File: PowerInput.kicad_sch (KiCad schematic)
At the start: 26 parts, among them J3 USB_C_Receptacle_USB2.0_16P, Q1 STL6P3LLH6, Q2 STL6P3LLH6, U4 STUSB4500QTR

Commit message: this is probably a fire hazard
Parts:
- added U5: INA180A3, Package_TO_SOT_SMD:SOT-23-5, symbol Amplifier_Current:INA180A3
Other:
- note added: "not done, pull up"
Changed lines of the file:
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@@
 	(generator_version "9.0")
 	(paper "A4")
+	(text "not done, pull up"
+		(exclude_from_sim no)
+		(at 96.774 130.302 0)
+		(effects
+			(font
+				(size 1.27 1.27)
+			)
+		)
+	)
 	(junction
 		(at 105.41 97.79)
@@
 					(unit 1)
 				)
+			)
+		)
+	)
+	(symbol
+		(lib_id "Amplifier_Current:INA180A3")
+		(at 257.81 149.86 0)
+		(unit 1)
+		(exclude_from_sim no)
+		(in_bom yes)
+		(on_board yes)
+		(dnp no)
+		(fields_autoplaced yes)
+		(property "Reference" "U5"
+			(at 269.24 143.4398 0)
+			(effects
+				(font
+					(size 1.27 1.27)
+				)
+			)
+		)
+		(property "Value" "INA180A3"
+			(at 269.24 145.9798 0)
+			(effects
+				(font
+					(size 1.27 1.27)
+				)
+			)
+		)
+		(property "Footprint" "Package_TO_SOT_SMD:SOT-23-5"
+			(at 259.08 148.59 0)
+			(effects
+				(font
+					(size 1.27 1.27)
+				)
+				(hide yes)
+			)
+		)
+		(property "Datasheet" "http://www.ti.com/lit/ds/symlink/ina180.pdf"
+			(at 261.62 146.05 0)
+			(effects
+				(font
+					(size 1.27 1.27)
+				)
+				(hide yes)
+			)
+		)
+		(property "Description" "Current Sense Amplifier, 1 Circuit, Rail-to-Rail, 26V, Gain 100 V/V, SOT-23-5"
+			(at 257.81 149.86 0)
+			(effects
+				(font
+					(size 1.27 1.27)
+				)
+				(hide yes)
+			)
+		)
+		(pin "2"
+		)
+		(pin "5"
+		)
+		(pin "1"
+		)
+		(pin "3"
+		)
+		(pin "4"
+		)
+		(instances
+			(project ""
+				(path "/7a2fe565-c497-4bbc-a9ac-a0a5f0f67328/4de8efdc-a788-4a67-8536-a7c2640bcc0c"
+					(reference "U5")
+					(unit 1)
+				)

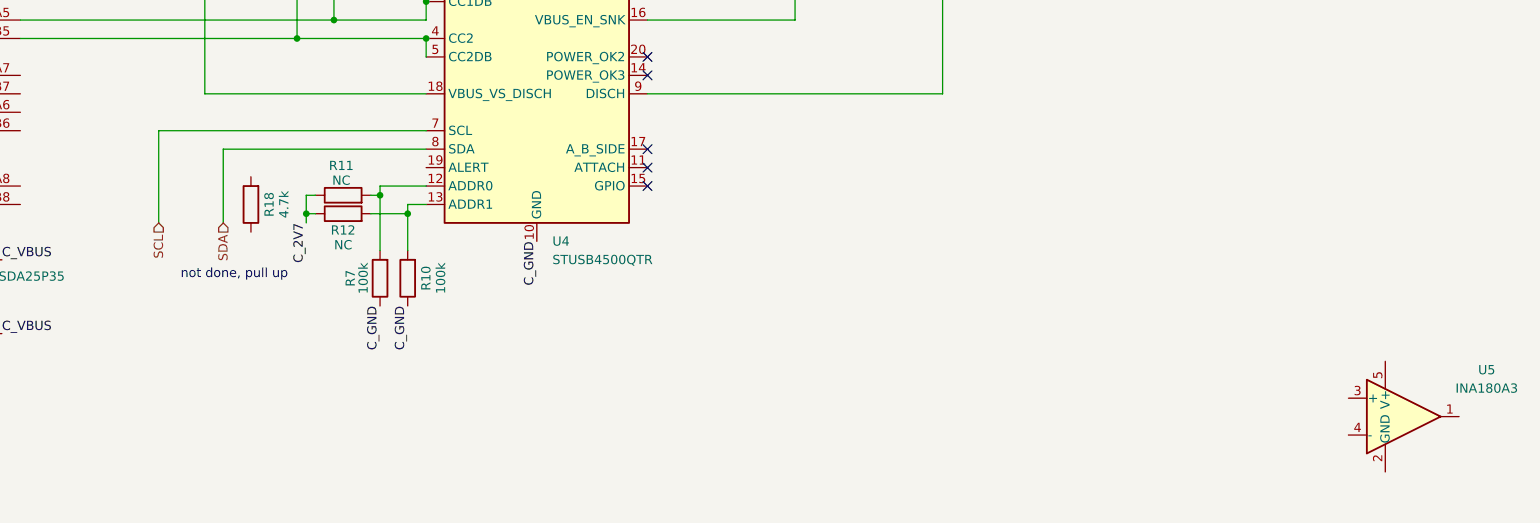
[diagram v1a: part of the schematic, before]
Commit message: add buck
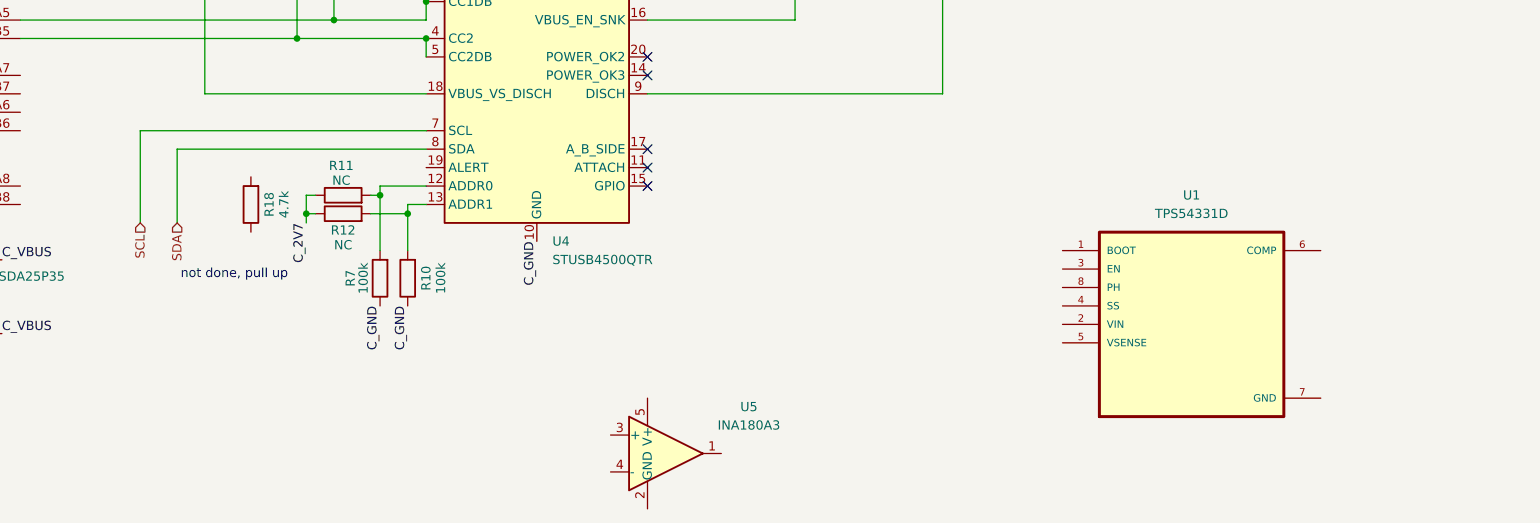
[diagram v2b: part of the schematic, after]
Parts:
- added U1: TPS54331D, TPS54331D:SOIC127P599X175-8N, symbol TPS54331D:TPS54331D
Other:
- moved on the sheet: U5
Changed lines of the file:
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@@
 	(wire
 		(pts
-			(xy 86.36 110.49) (xy 123.19 110.49)
+			(xy 83.82 110.49) (xy 123.19 110.49)
 		)
 		(stroke
@@
 	(wire
 		(pts
-			(xy 95.25 123.19) (xy 95.25 113.03)
+			(xy 88.9 123.19) (xy 88.9 113.03)
 		)
 		(stroke
@@
 	(wire
 		(pts
-			(xy 95.25 113.03) (xy 123.19 113.03)
+			(xy 88.9 113.03) (xy 123.19 113.03)
 		)
 		(stroke
@@
 	(wire
 		(pts
-			(xy 86.36 123.19) (xy 86.36 110.49)
+			(xy 83.82 123.19) (xy 83.82 110.49)
 		)
 		(stroke
@@
 	(hierarchical_label "SDA"
 		(shape input)
-		(at 95.25 123.19 270)
+		(at 88.9 123.19 270)
 		(effects
 			(font
@@
 	(hierarchical_label "SCL"
 		(shape input)
-		(at 86.36 123.19 270)
+		(at 83.82 123.19 270)
 		(effects
 			(font
@@
 	)
 	(symbol
+		(lib_id "TPS54331D:TPS54331D")
+		(at 228.6 137.16 0)
+		(unit 1)
+		(exclude_from_sim no)
+		(in_bom yes)
+		(on_board yes)
+		(dnp no)
+		(fields_autoplaced yes)
+		(property "Reference" "U1"
+			(at 228.6 119.38 0)
+			(effects
+				(font
+					(size 1.27 1.27)
+				)
+			)
+		)
+		(property "Value" "TPS54331D"
+			(at 228.6 121.92 0)
+			(effects
+				(font
+					(size 1.27 1.27)
+				)
+			)
+		)
+		(property "Footprint" "TPS54331D:SOIC127P599X175-8N"
+			(at 228.6 137.16 0)
+			(effects
+				(font
+					(size 1.27 1.27)
+				)
+				(justify bottom)
+				(hide yes)
+			)
+		)
+		(property "Datasheet" ""
+			(at 228.6 137.16 0)
+			(effects
+				(font
+					(size 1.27 1.27)
+				)
+				(hide yes)
+			)
+		)
+		(property "Description" ""
+			(at 228.6 137.16 0)
+			(effects
+				(font
+					(size 1.27 1.27)
+				)
+				(hide yes)
+			)
+		)
+		(property "MF" "Texas Instruments"
+			(at 228.6 137.16 0)
+			(effects
+				(font
+					(size 1.27 1.27)
+				)
+				(justify bottom)
+				(hide yes)
+			)
+		)
+		(property "Description_1" "3.5V to 28V Input, 3A, 570kHz Step-Down Converter with Eco-mode"
+			(at 228.6 137.16 0)
+			(effects
+				(font
+					(size 1.27 1.27)
+				)
+				(justify bottom)
+				(hide yes)
+			)
+		)
+		(property "Package" "SOIC-8 Texas Instruments"
+			(at 228.6 137.16 0)
+			(effects
+				(font
+					(size 1.27 1.27)
+				)
+				(justify bottom)
+				(hide yes)
+			)
+		)
+		(property "Price" "None"
+			(at 228.6 137.16 0)
+			(effects
+				(font
+					(size 1.27 1.27)
+				)
+				(justify bottom)
+				(hide yes)
+			)
+		)
+		(property "SnapEDA_Link" "https://www.snapeda.com/parts/TPS54331D/Texas+Instruments/view-part/?ref=snap"
+			(at 228.6 137.16 0)
+			(effects
+				(font
+					(size 1.27 1.27)
+				)
+				(justify bottom)
+				(hide yes)
+			)
+		)
+		(property "MP" "TPS54331D"
+			(at 228.6 137.16 0)
+			(effects
+				(font
+					(size 1.27 1.27)
+				)
+				(justify bottom)
+				(hide yes)
+			)
+		)
+		(property "Availability" "In Stock"
+			(at 228.6 137.16 0)
+			(effects
+				(font
+					(size 1.27 1.27)
+				)
+				(justify bottom)
+				(hide yes)
+			)
+		)
+		(property "Check_prices" "https://www.snapeda.com/parts/TPS54331D/Texas+Instruments/view-part/?ref=eda"
+			(at 228.6 137.16 0)
+			(effects
+				(font
+					(size 1.27 1.27)
+				)
+				(justify bottom)
+				(hide yes)
+			)
+		)
+		(pin "1"
+		)
+		(pin "7"
+		)
+		(pin "6"
+		)
+		(pin "8"
+		)
+		(pin "2"
+		)
+		(pin "4"
+		)
+		(pin "5"
+		)
+		(pin "3"
+		)
+		(instances
+			(project ""
+				(path "/7a2fe565-c497-4bbc-a9ac-a0a5f0f67328/4de8efdc-a788-4a67-8536-a7c2640bcc0c"
+					(reference "U1")
+					(unit 1)
+				)
+			)
+		)
+	)
+	(symbol
 		(lib_id "Interface_USB:STUSB4500QTR")
 		(at 138.43 102.87 0)
@@
 	(symbol
 		(lib_id "Amplifier_Current:INA180A3")
-		(at 257.81 149.86 0)
+		(at 156.21 154.94 0)
 		(unit 1)
 		(exclude_from_sim no)
@@
 		(fields_autoplaced yes)
 		(property "Reference" "U5"
-			(at 269.24 143.4398 0)
+			(at 167.64 148.5198 0)
 			(effects
 				(font
@@
 		)
 		(property "Value" "INA180A3"
-			(at 269.24 145.9798 0)
+			(at 167.64 151.0598 0)
 			(effects
 				(font
@@
 		)
 		(property "Footprint" "Package_TO_SOT_SMD:SOT-23-5"
-			(at 259.08 148.59 0)
+			(at 157.48 153.67 0)
 			(effects
 				(font
@@
 		)
 		(property "Datasheet" "http://www.ti.com/lit/ds/symlink/ina180.pdf"
-			(at 261.62 146.05 0)
+			(at 160.02 151.13 0)
 			(effects
 				(font
@@
 		)
 		(property "Description" "Current Sense Amplifier, 1 Circuit, Rail-to-Rail, 26V, Gain 100 V/V, SOT-23-5"
-			(at 257.81 149.86 0)
-			(effects
-				(font
+			(at 156.21 154.94 0)
+			(effects
+				(font

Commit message: fire hazard!!!
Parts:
- removed U1: TPS54331D, TPS54331D:SOIC127P599X175-8N, symbol TPS54331D:TPS54331D
- removed U5: INA180A3, Package_TO_SOT_SMD:SOT-23-5, symbol Amplifier_Current:INA180A3
- added R, R9: 4.7k, symbol Device:R
- renumbered C18 to C, D1 to D, D3 to D, D2 to D, D4 to D, Q1 to Q, R7 to R
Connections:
- net C_2V7: now also R11.2, R12.2; no longer R11.1, R12.1
- net GND: now also J3.S1 (SHIELD)
- net SCL: now also R18.1
- net SDA: now also R9.1
- net at R.2, U4.12 (ADDR0): now also R11.1; no longer R11.2
- net at R10.2, U4.13 (ADDR1): now also R12.1; no longer R12.2
- net ALERT: now reaches U4.19 (ALERT)
- net ALERT: now also R.1
- net USB_D+: now reaches J3.A6 (D+)
- net USB_D+: now also J3.B6 (D+)
- net USB_D-: now reaches J3.A7 (D-)
- net USB_D-: now also J3.B7 (D-)
- net V_MCU: now reaches R18.2
- net V_MCU: now also R.2, R9.2
- net VCC renamed VOUT
- no-connect marks 5 -> 7
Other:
- note removed: "not done, pull up"
- moved on the sheet: R, R10, R11, R12, R17

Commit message: more work
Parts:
- added D1: D, symbol Device:D
- renumbered C to C24, D to D5, D to D6, D to D7, D to D8, Q to Q3, R to R23, R to R24
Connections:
- net VOUT: now also D1.1 (K); no longer C23.2, D8.1 (K), Q2.1, Q2.2, Q2.3, R17.1
- new net C_Vsnk: C23.2, D1.2 (A), D8.1 (K), Q2.1, Q2.2, Q2.3, R17.1
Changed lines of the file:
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@@
 	)
 	(label "C_GND"
-		(at 271.78 43.18 270)
+		(at 266.7 58.42 270)
 		(effects
 			(font
@@
 			)
 			(justify left bottom)
-		)
-	)
-	(hierarchical_label "VOUT"
-		(shape input)
-		(at 260.35 43.18 0)
-		(effects
-			(font
-				(size 1.27 1.27)
-			)
-			(justify left)
 		)
 	)
@@
 		)
 	)
+	(hierarchical_label "VOUT"
+		(shape input)
+		(at 267.97 43.18 0)
+		(effects
+			(font
+				(size 1.27 1.27)
+			)
+			(justify left)
+		)
+	)
 	(hierarchical_label "V_MCU"
 		(shape input)
@@
 	(hierarchical_label "GND"
 		(shape input)
-		(at 271.78 43.18 0)
+		(at 266.7 58.42 0)
 		(effects
 			(font
@@
 		(dnp no)
 		(fields_autoplaced yes)
-		(property "Reference" "Q"
+		(property "Reference" "Q?"
 			(at 171.45 36.83 90)
 			(effects
@@
 				(path "/7a2fe565-c497-4bbc-a9ac-a0a5f0f67328/384eb686-8507-4fe7-b380-c0d2ed53ff95"
 					(reference "Q3")
+					(unit 1)
+				)
+				(path "/7a2fe565-c497-4bbc-a9ac-a0a5f0f67328/4de8efdc-a788-4a67-8536-a7c2640bcc0c"
+					(reference "Q?")
 					(unit 1)
 				)
@@
 		(on_board yes)
 		(dnp no)
-		(property "Reference" "D"
+		(property "Reference" "D?"
 			(at 103.632 81.534 0)
 			(effects
@@
 					(unit 1)
 				)
+				(path "/7a2fe565-c497-4bbc-a9ac-a0a5f0f67328/4de8efdc-a788-4a67-8536-a7c2640bcc0c"
+					(reference "D?")
+					(unit 1)
+				)
 				(path "/7a2fe565-c497-4bbc-a9ac-a0a5f0f67328/8214f10f-2c6e-4274-a3ba-6a32c80ab6b1"
 					(reference "D11")
@@
 		(on_board yes)
 		(dnp no)
-		(property "Reference" "R"
+		(property "Reference" "R?"
 			(at 111.506 144.78 90)
 			(effects
@@
 					(unit 1)
 				)
+				(path "/7a2fe565-c497-4bbc-a9ac-a0a5f0f67328/4de8efdc-a788-4a67-8536-a7c2640bcc0c"
+					(reference "R?")
+					(unit 1)
+				)
 				(path "/7a2fe565-c497-4bbc-a9ac-a0a5f0f67328/8214f10f-2c6e-4274-a3ba-6a32c80ab6b1"
 					(reference "R38")
@@
 		(on_board yes)
 		(dnp no)
-		(property "Reference" "C"
+		(property "Reference" "C?"
 			(at 60.96 143.002 90)
 			(effects
@@
 					(unit 1)
 				)
+				(path "/7a2fe565-c497-4bbc-a9ac-a0a5f0f67328/4de8efdc-a788-4a67-8536-a7c2640bcc0c"
+					(reference "C?")
+					(unit 1)
+				)
 				(path "/7a2fe565-c497-4bbc-a9ac-a0a5f0f67328/8214f10f-2c6e-4274-a3ba-6a32c80ab6b1"
 					(reference "C30")
@@
 		(on_board yes)
 		(dnp no)
-		(property "Reference" "R"
+		(property "Reference" "R?"
 			(at 100.838 123.19 0)
 			(effects
@@
 					(unit 1)
 				)
+				(path "/7a2fe565-c497-4bbc-a9ac-a0a5f0f67328/4de8efdc-a788-4a67-8536-a7c2640bcc0c"
+					(reference "R?")
+					(unit 1)
+				)
 				(path "/7a2fe565-c497-4bbc-a9ac-a0a5f0f67328/8214f10f-2c6e-4274-a3ba-6a32c80ab6b1"
 					(reference "R37")
@@
 		(dnp no)
 		(fields_autoplaced yes)
-		(property "Reference" "D"
+		(property "Reference" "D?"
 			(at 85.09 68.5799 90)
 			(effects
@@
 					(unit 1)
 				)
+				(path "/7a2fe565-c497-4bbc-a9ac-a0a5f0f67328/4de8efdc-a788-4a67-8536-a7c2640bcc0c"
+					(reference "D?")
+					(unit 1)
+				)
 				(path "/7a2fe565-c497-4bbc-a9ac-a0a5f0f67328/8214f10f-2c6e-4274-a3ba-6a32c80ab6b1"
 					(reference "D10")
@@
 		(on_board yes)
 		(dnp no)
-		(property "Reference" "D"
+		(property "Reference" "D?"
 			(at 60.96 132.08 0)
 			(effects
@@
 					(unit 1)
 				)
+				(path "/7a2fe565-c497-4bbc-a9ac-a0a5f0f67328/4de8efdc-a788-4a67-8536-a7c2640bcc0c"
+					(reference "D?")
+					(unit 1)
+				)
 				(path "/7a2fe565-c497-4bbc-a9ac-a0a5f0f67328/8214f10f-2c6e-4274-a3ba-6a32c80ab6b1"
 					(reference "D9")
@@
 		(dnp no)
 		(fields_autoplaced yes)
-		(property "Reference" "D"
+		(property "Reference" "D?"
 			(at 251.46 48.2599 90)
 			(effects
@@
 					(unit 1)
 				)
+				(path "/7a2fe565-c497-4bbc-a9ac-a0a5f0f67328/4de8efdc-a788-4a67-8536-a7c2640bcc0c"
+					(reference "D?")
+					(unit 1)
+				)
 				(path "/7a2fe565-c497-4bbc-a9ac-a0a5f0f67328/8214f10f-2c6e-4274-a3ba-6a32c80ab6b1"
 					(reference "D12")
@@
 					(unit 1)
 				)
+			)
+		)
+	)
+	(symbol
+		(lib_id "Device:D")
+		(at 264.16 43.18 180)
+		(unit 1)
+		(exclude_from_sim no)
+		(in_bom yes)
+		(on_board yes)
+		(dnp no)
+		(fields_autoplaced yes)
+		(property "Reference" "D1"
+			(at 264.16 36.83 0)
+			(effects
+				(font
+					(size 1.27 1.27)
+				)
+			)
+		)
+		(property "Value" "D"
+			(at 264.16 39.37 0)
+			(effects
+				(font
+					(size 1.27 1.27)
+				)
+			)
+		)
+		(property "Footprint" ""
+			(at 264.16 43.18 0)
+			(effects
+				(font
+					(size 1.27 1.27)
+				)
+				(hide yes)
+			)
+		)
+		(property "Datasheet" "~"
+			(at 264.16 43.18 0)
+			(effects
+				(font
+					(size 1.27 1.27)
+				)
+				(hide yes)
+			)
+		)
+		(property "Description" "Diode"
+			(at 264.16 43.18 0)
+			(effects
+				(font
+					(size 1.27 1.27)
+				)
+				(hide yes)
+			)
+		)
+		(property "Sim.Device" "D"
+			(at 264.16 43.18 0)
+			(effects
+				(font
+					(size 1.27 1.27)
+				)
+				(hide yes)
+			)
+		)
+		(property "Sim.Pins" "1=K 2=A"
+			(at 264.16 43.18 0)
+			(effects
+				(font
+					(size 1.27 1.27)
+				)
+				(hide yes)
+			)
+		)
+		(pin "1"
+		)
+		(pin "2"
+		)
+		(instances
+			(project ""
+				(path "/7a2fe565-c497-4bbc-a9ac-a0a5f0f67328/384eb686-8507-4fe7-b380-c0d2ed53ff95"
+					(reference "D2")
+					(unit 1)
+				)
+				(path "/7a2fe565-c497-4bbc-a9ac-a0a5f0f67328/4de8efdc-a788-4a67-8536-a7c2640bcc0c"
+					(reference "D1")
+					(unit 1)
+				)
+				(path "/7a2fe565-c497-4bbc-a9ac-a0a5f0f67328/8214f10f-2c6e-4274-a3ba-6a32c80ab6b1"
+					(reference "D3")
+					(unit 1)
+				)
+				(path "/7a2fe565-c497-4bbc-a9ac-a0a5f0f67328/c2ea810b-3e14-4f17-8acf-ca943e03b0c4"
+					(reference "D4")
+					(unit 1)
+				)

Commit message: Complete PD circuts
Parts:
- added C1: C, symbol Device:C
- added VR1: XL6019, XL6009:DPAK170P1435X465-6N, symbol XL6009:XL6009
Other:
- moved on the sheet: C19, C20, C21, C22, C23, C24, D1, D5, D6, D7, D8, J3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
